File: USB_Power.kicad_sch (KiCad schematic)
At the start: 30 parts, among them J6 USB_C_Receptacle_USB2.0_16P, J8 Conn_01x04_Pin, U10 BQ21080YBGR, U4 RT6150BGQW

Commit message: PCB updates
Update miscellaneous.kicad_sch to add new fiducial symbol and replace existing fiducial references

- Added a new fiducial symbol "BC_Miscellaneous:Fiducial" with ground
- Updated references in the schematic to point to the new fiducial symbol.

- Changed the DNP (Do Not Place) property for components U13 and U6 from 'no' to 'yes' to prevent placement on the PCB.
- Updated the footprint property for U13 to "BC_Memory:W25Q" to reflect the correct component footprint.
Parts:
- added C43: 4u7, Capacitor_SMD:C_0402_1005Metric, symbol Device:C
- J6: footprint Connector_USB:USB_C_Receptacle_HRO_TYPE-C-31-M-12 -> BC_Miscellaneous:USB_C_Receptacle_HRO_TYPE-C-31-M-12
- TH2: footprint Resistor_THT:R_Axial_DIN0204_L3.6mm_D1.6mm_P2.54mm_Vertical -> Resistor_SMD:R_0603_1608Metric_Pad0.98x0.95mm_HandSolder
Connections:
- net GND: now also C43.2
- net at BT1.1 (+), U10.C2 (BAT): now also C43.1
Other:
- moved on the sheet: BT1

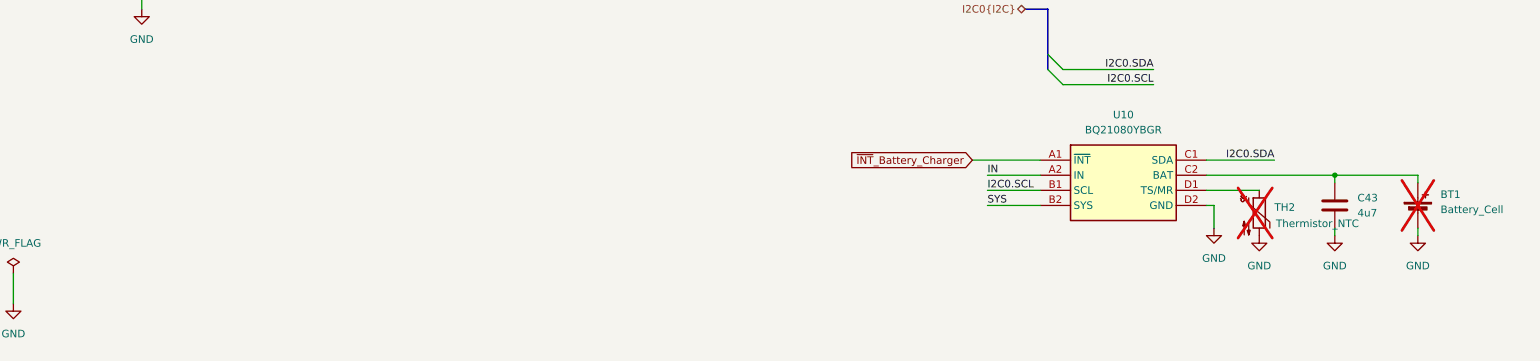
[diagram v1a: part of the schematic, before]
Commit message: Update subproject reference for kicad-libs to latest commit fe3e1e7
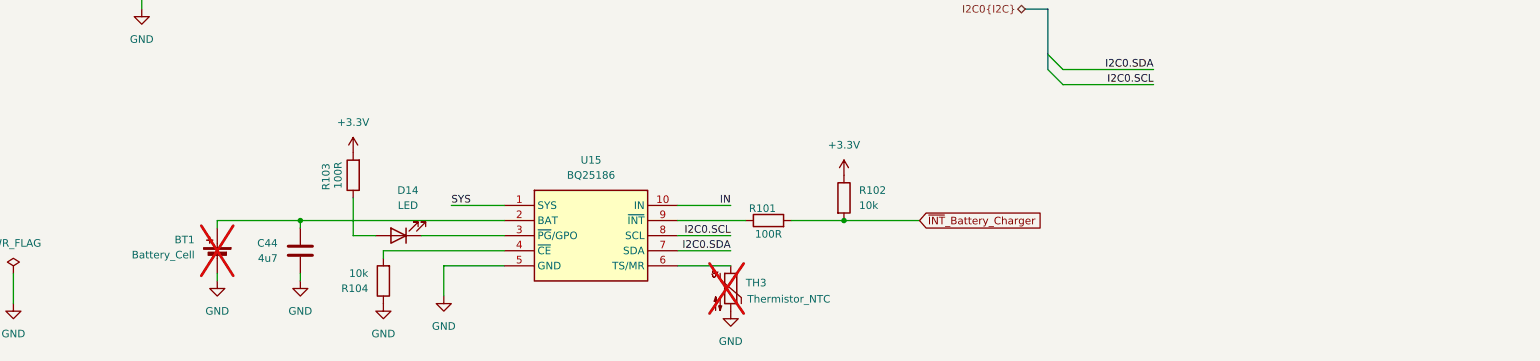
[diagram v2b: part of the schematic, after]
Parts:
- removed C43: 4u7, Capacitor_SMD:C_0402_1005Metric, symbol Device:C
- removed TH2: Thermistor_NTC, Resistor_SMD:R_0603_1608Metric_Pad0.98x0.95mm_HandSolder, symbol Device:Thermistor_NTC
- removed U10: BQ21080YBGR, BC_Power:BGA8C40P2X4_100X155X50, symbol BC_Power:BQ21080YBGR
- added C44: 4u7, Capacitor_SMD:C_0402_1005Metric, symbol Device:C
- added D14: LED, Diode_SMD:D_0603_1608Metric, symbol Device:LED
- added R101, R103: 100R, Resistor_SMD:R_0402_1005Metric, symbol Device:R
- added R102, R104: 10k, Resistor_SMD:R_0402_1005Metric, symbol Device:R
- added TH3: Thermistor_NTC, Resistor_SMD:R_0603_1608Metric_Pad0.98x0.95mm_HandSolder, symbol Device:Thermistor_NTC
- added U15: BQ25186, BC_Power:BQ25186DLHR_SON40P220X200X80-11N, symbol BC_Power:BQ25186DLHR
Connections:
- net +3.3V: now also R102.1, R103.2
- net GND: now also C44.2, R104.1, TH3.2, U15.11 (GND), U15.5 (GND)
- net I2C0.SCL: now also U15.8 (SCL)
- net I2C0.SDA: now also U15.7 (SDA)
- net IN: now also U15.10 (IN)
- net SYS: now also U15.1 (SYS)
- net ~{INT}_Battery_Charger: now also R101.2, R102.2
- net at BT1.1 (+): now also C44.1, U15.2 (BAT)
- new net: D14.2 (A), R103.1
- new net: R104.2, U15.4 (~{CE})
- new net: TH3.1, U15.6 (TS/MR)
- new net: R101.1, U15.9 (~{INT})
- new net: D14.1 (K), U15.3 (~{PG}/GPO)

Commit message: send to production. v0.1, making jobset for export
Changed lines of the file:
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@@
 	(generator_version "10.0")
 	(paper "A4")
+	(title_block
+		(rev "${Revision}")
+	)
 	(junction
 		(at 115.57 36.83)
@@
 		(lib_id "Device:R")
 		(at 168.91 147.32 0)
+		(mirror y)
 		(unit 1)
 		(body_style 1)
@@
 		(in_pos_files yes)
 		(dnp no)
-		(fields_autoplaced yes)
 		(property "Reference" "R102"
-			(at 171.45 146.0499 0)
+			(at 166.37 146.0499 0)
 			(show_name no)
 			(do_not_autoplace no)
@@
 		)
 		(property "Value" "10k"
-			(at 171.45 148.5899 0)
+			(at 166.37 148.5899 0)
 			(show_name no)
 			(do_not_autoplace no)
@@
 		)
 		(property "Footprint" "Resistor_SMD:R_0402_1005Metric"
-			(at 167.132 147.32 90)
-			(hide yes)
-			(show_name no)
+			(at 170.688 147.32 90)
+			(hide yes)
+			(show_name no)
